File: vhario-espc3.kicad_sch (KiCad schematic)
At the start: 56 parts, among them J1 USB_C, J2 Battery, Q1 AO3401A, Q2 2N7002, SW1 RST, SW2 DBG, SW3 PWR, SW4 PCCA, U1 cjmcu117, U2 MCP73831-2-OT, U3 espc3fn4, U4 74HC240PWR, U5 TLV75533PDBV

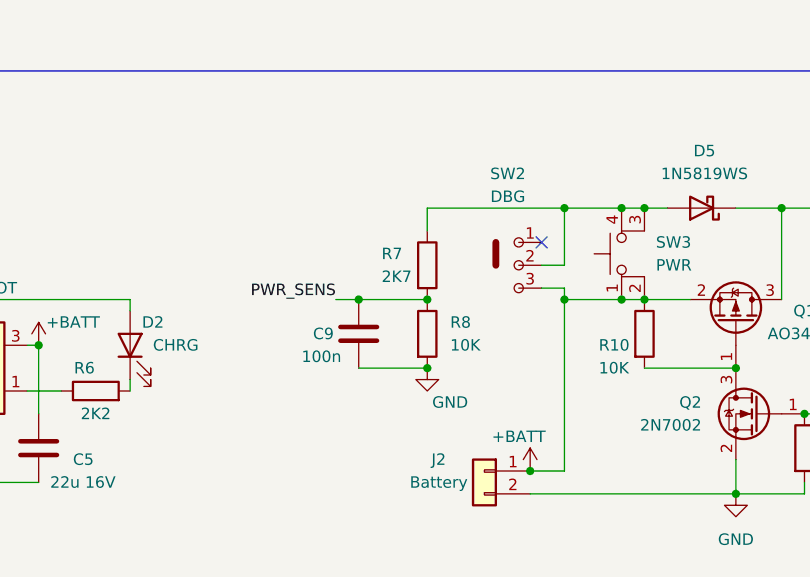
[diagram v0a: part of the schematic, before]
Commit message: change flash/dbg jumper options
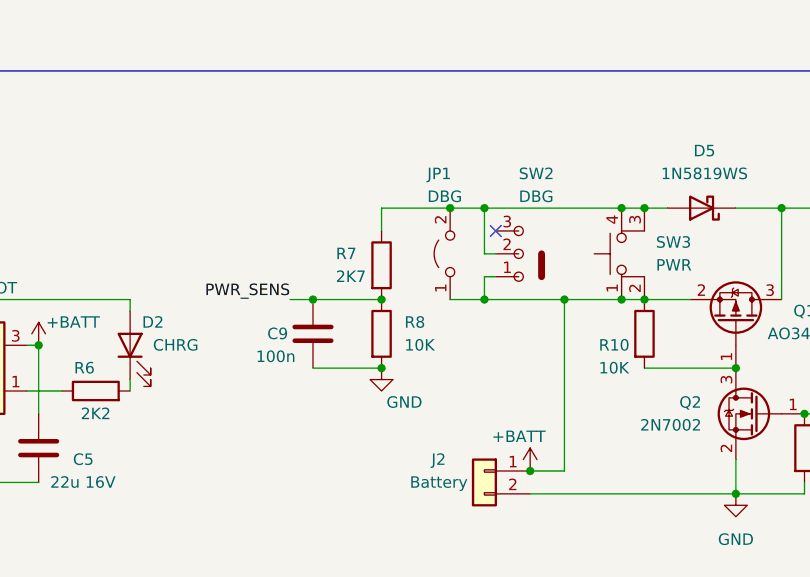
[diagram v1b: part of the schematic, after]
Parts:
- added JP1: DBG, 0-vhario-espc3:PinSocket_1x02_P2.54mm_Vertical, symbol 0-vhario-espc3:Jumper_2_Open
- SW2: footprint 0-vhario-espc3:sk12d07vg3 -> 0-vhario-espc3:SW_SPDT_PCM12
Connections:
- net +BATT: now also SW2.1 (A), JP1.1 (A); no longer SW2.3 (C)
- net at D5.2 (A), R7.1, SW2.2 (B)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: now also JP1.2 (B)
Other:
- moved on the sheet: C9, R7, R8, SW2
